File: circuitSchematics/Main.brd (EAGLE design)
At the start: 45.7 x 63.5 mm, 9 parts, among them J1 RASPBERRYPI-40-PIN-GPIO_PTH, J2 Heating_element, Q1 60V/32A/35mΩ, U1 DS18B20

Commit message: Updated circuit schematics
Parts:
- removed J2: Heating_element, SparkFun-Connectors:1X02_BIG
- removed Q1: 60V/32A/35mΩ, SparkFun-DiscreteSemi:TO220V
- removed ULN1: (no value), SparkFun-IC-Special-Function:DIL18
- removed VR1: 10k, SparkFun-Resistors:TRIMPOT-PTH-3386U
- added 59630, HEATING_ELEMENT: (no value), SparkFun-Connectors:1X02_BIG
- added FQP30N06L: 60V/32A/35mΩ, SparkFun-DiscreteSemi:TO220V
- added I2C_DISPLAY: (no value), SparkFun-Connectors:1X04
- added R2: 10k, SparkFun-Resistors:AXIAL-0.3
- added ULN2803A: (no value), SparkFun-IC-Special-Function:DIL18
- moved J1 83.0 mm to (88.9, 40.6)
- moved U1 64.3 mm to (57.1, 67.3)
- moved 28BYJ-48 49.3 mm to (57.1, 16.5), flipped to the bottom, turned to 0 degrees
- moved R1 33.8 mm to (54.6, 45.7), flipped to the bottom, turned to 0 degrees
- moved PS 23.2 mm to (43.2, 64.8), turned to 90 degrees
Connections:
- net N$1 renamed DQ
- removed net N$12: J1.36, ULN1.4
- removed net N$7: J1.11, VR1.2
- removed net VCC_12V: J2.P$1, PS.P2
- new net 12V: HEATING_ELEMENT.P$1, PS.P2
- new net 3V3: J1.1, R2.P$1
- new net N$5: J1.37, ULN2803A.4
- new net SCL: I2C_DISPLAY.4, J1.5
- new net SDA: I2C_DISPLAY.3, J1.3
- new net WS: 59630.P$1, J1.11, R2.P$2
- net 5V: now also I2C_DISPLAY.2, ULN2803A.10; no longer ULN1.10, VR1.1
- net GND: now also 59630.P$2, FQP30N06L.3, I2C_DISPLAY.1, ULN2803A.9; no longer J1.1, Q1.3, ULN1.9, VR1.3
- net N$10: now also J1.33, ULN2803A.2; no longer J1.32, ULN1.2
- net N$13: now also ULN2803A.18; no longer ULN1.18
- net N$14: now also ULN2803A.17; no longer ULN1.17
- net N$15: now also ULN2803A.16; no longer ULN1.16
- net N$16: now also ULN2803A.15; no longer ULN1.15
- net N$2: now also ULN2803A.1; no longer ULN1.1
- net N$3: now also FQP30N06L.1; no longer Q1.1
- net N$4: now also J1.35, ULN2803A.3; no longer J1.33, ULN1.3
- net N$8: now also FQP30N06L.2, HEATING_ELEMENT.P$2; no longer J2.P$2, Q1.2
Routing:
- net N$3: track 26.0 -> 92.0 mm
- net GND: track 267.2 -> 203.4 mm
- net N$8: track 71.5 -> 12.9 mm
- net N$12: track 55.9 -> 0.00 mm
- net WS: track 0.00 -> 55.0 mm
- net 3V3: track 0.00 -> 54.8 mm
- net N$7: track 51.8 -> 0.00 mm
- net 5V: track 107.7 -> 146.1 mm
- net DQ: track 87.5 -> 58.9 mm
- net N$13: track 17.7 -> 43.8 mm
- net N$5: track 0.00 -> 22.0 mm
- net N$14: track 20.1 -> 41.1 mm
- net N$2: track 41.6 -> 22.0 mm
- net SDA: track 0.00 -> 17.2 mm
- net SCL: track 0.00 -> 14.7 mm
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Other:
- board size 45.7 x 63.5 mm -> 65.7 x 66 mm

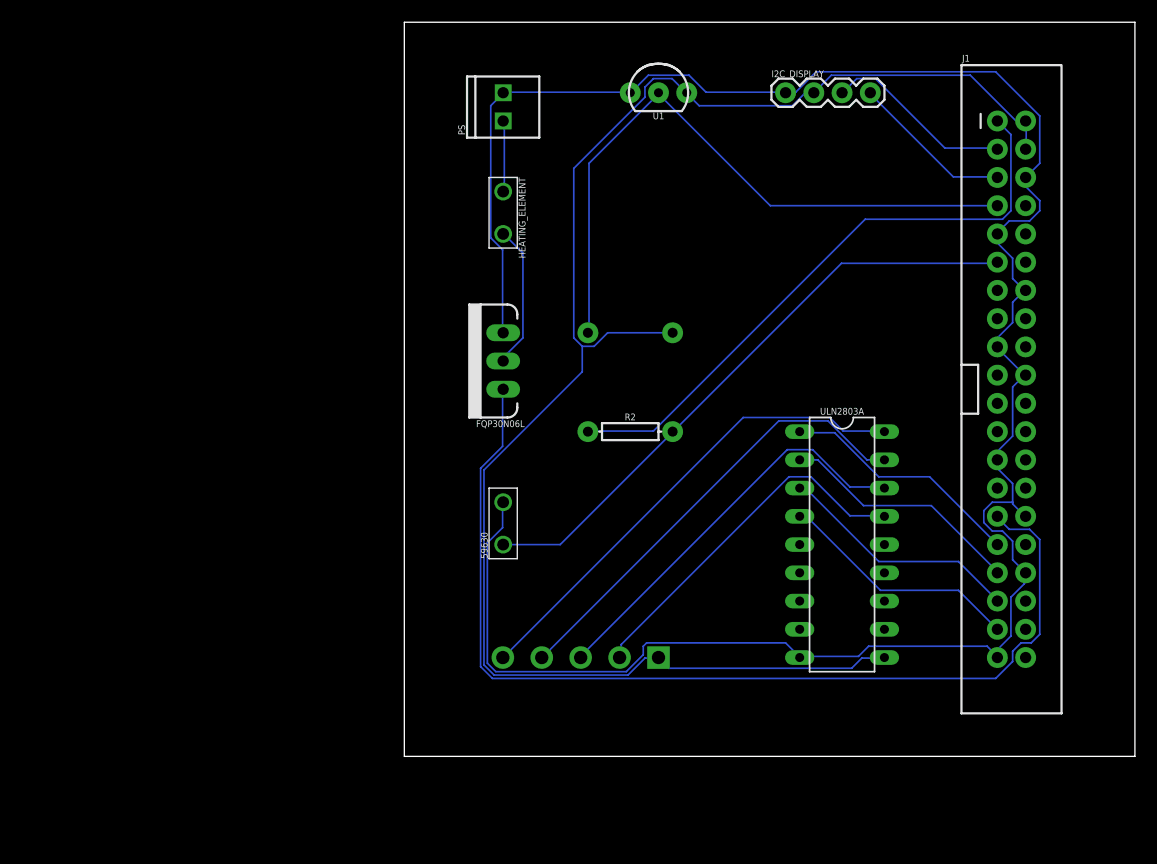
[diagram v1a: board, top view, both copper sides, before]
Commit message: Added float sensor and I2C LCD
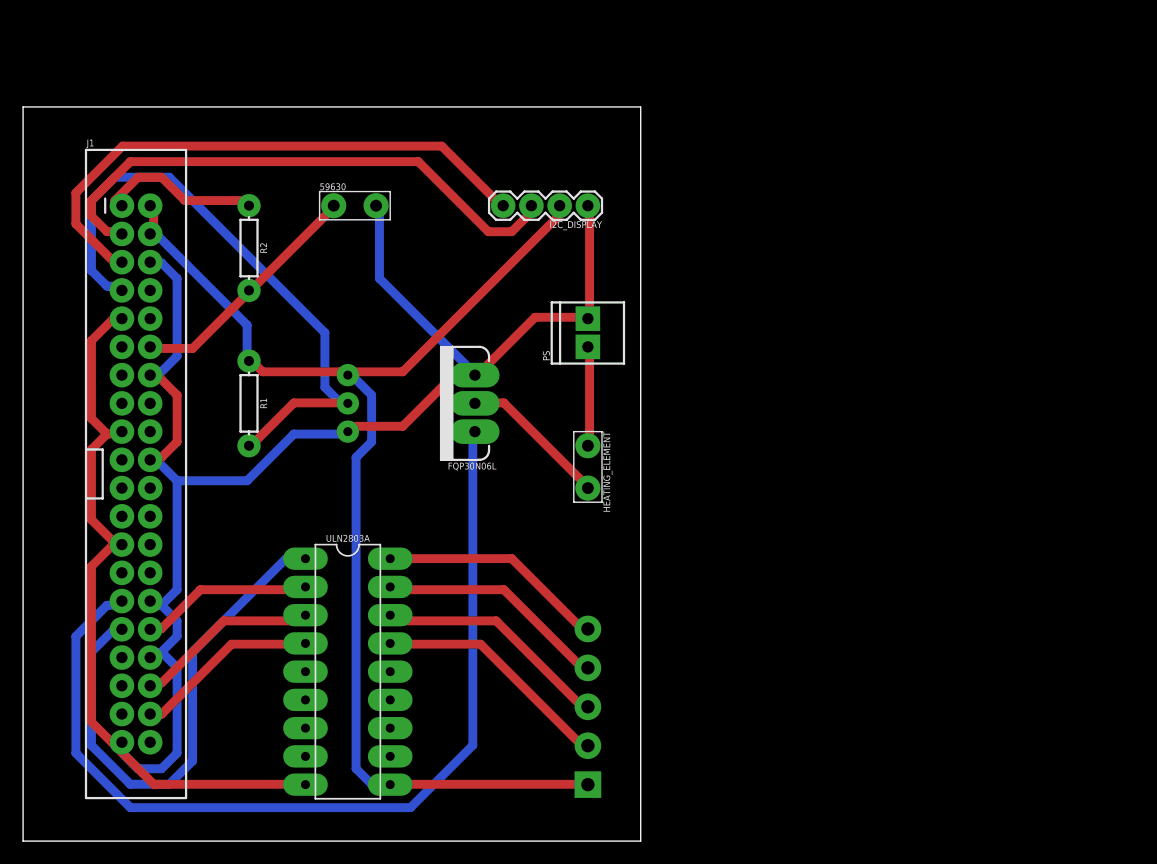
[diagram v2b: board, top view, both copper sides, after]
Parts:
- moved J1 79.1 mm to (10.2, 33.0)
- moved ULN2803A 45.9 mm to (29.2, 15.2)
- moved U1 39.5 mm to (29.2, 39.4), flipped to the bottom, turned to 90 degrees
- moved R2 38.1 mm to (20.3, 53.3), turned to 270 degrees
- moved R1 34.9 mm to (20.3, 39.4), flipped to the top, turned to 270 degrees
- moved 59630 34.1 mm to (27.9, 57.1), turned to 0 degrees
- moved HEATING_ELEMENT 24.1 mm to (50.8, 35.6)
- moved PS 21.7 mm to (50.8, 44.5)
- moved I2C_DISPLAY 20.5 mm to (50.8, 57.1), turned to 180 degrees
- moved 28BYJ-48 13.1 mm to (50.8, 5.08), turned to 90 degrees
- moved FQP30N06L 4.58 mm to (40.6, 39.4)
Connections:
- net N$10: now also J1.32; no longer J1.33
- net N$4: now also J1.36; no longer J1.35
- net N$5: now also J1.38; no longer J1.37
- net WS: now also J1.12; no longer J1.11
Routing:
- net 3V3: track 54.8 -> 14.9 mm
- net SCL: track 14.7 -> 50.7 mm
- net 5V: track 146.1 -> 112.6 mm
- net WS: track 55.0 -> 21.9 mm
- net SDA: track 17.2 -> 50.0 mm
- net N$2: track 22.0 -> 46.9 mm
- net N$13: track 43.8 -> 20.4 mm
- net N$14: track 41.1 -> 20.7 mm
- net N$15: track 36.6 -> 21.2 mm
- net N$16: track 32.6 -> 21.6 mm
- net N$3: track 92.0 -> 84.2 mm
- net N$10: track 22.0 -> 15.5 mm
- net N$5: track 22.0 -> 16.6 mm
- net N$4: track 22.0 -> 16.6 mm
- net DQ: track 58.9 -> 55.4 mm
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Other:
- board size 65.7 x 66 mm -> 55.5 x 66 mm
